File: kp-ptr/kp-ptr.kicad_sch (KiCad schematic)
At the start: 31 parts, among them J1 ESP32_PROG_CON, U1 ESP32-S3, Y1 7M40000005-40MHz

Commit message: One step closer to perfection!
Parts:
- added R76, R77: 1k, Resistor_SMD:R_0402_1005Metric, symbol Device:R
- added R78: 100k, Resistor_SMD:R_0402_1005Metric, symbol Device:R
- added R79, R80: 10k, Resistor_SMD:R_0402_1005Metric, symbol Device:R
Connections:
- net +3V3: now also R78.2, R79.2, R80.2
- net LSM2_INT: now also R79.1
- net LSM_INT: now also R80.1
- net UART1_IN: now also R77.2; no longer U1.19 (GPIO14/ADC2_CH3)
- net UART1_OUT: now also R76.2; no longer U1.18 (GPIO13/ADC2_CH2)
- new net: R76.1, U1.18 (GPIO13/ADC2_CH2)
- new net: R77.1, R78.1, U1.19 (GPIO14/ADC2_CH3)
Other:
- moved on the sheet: R64, R65

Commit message: Parts renumbered! Noice!
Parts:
- renumbered C15 to C10, C4 to C11, C8 to C12, C9 to C13, C10 to C14, C11 to C15, C12 to C3, C13 to C4, C3 to C5, C5 to C6, C6 to C7, C7 to C8, C14 to C9, R79 to R1, R1 to R10, R2 to R11, R3 to R12, R4 to R13, R8 to R14, R5 to R15, R80 to R2, R64 to R3, R65 to R4, R6 to R5, R7 to R6, R76 to R7, R77 to R8, R78 to R9
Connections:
- net IGN1_DET: now also U1.12 (GPIO7/ADC1_CH6); no longer U1.10 (GPIO5/ADC1_CH4)
- net IGN1_EN: now also U1.17 (GPIO12/ADC2_CH1); no longer U1.16 (GPIO11/ADC2_CH0)
- net IGN3_DET: now also U1.10 (GPIO5/ADC1_CH4); no longer U1.12 (GPIO7/ADC1_CH6)
- net IGN3_EN: now also U1.16 (GPIO11/ADC2_CH0); no longer U1.14 (GPIO9/ADC1_CH8)
- net IGN4_EN: now also U1.14 (GPIO9/ADC1_CH8); no longer U1.17 (GPIO12/ADC2_CH1)

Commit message: Wersja produkcyjna v1
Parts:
- C1: value 4pF -> 3.3pF
- C2: value 5pF -> 4.7pF
- L2: value 2nH -> 3.9nH
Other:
- note added: "Optymalnie: 4pF - 1.8nH - 5pF"
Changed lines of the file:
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@@
     (stroke (width 0) (type default) (color 0 0 0 0))
+  )
+  (text "Optymalnie:\n4pF - 1.8nH - 5pF" (at 41.275 40.64 0)
+    (effects (font (size 1.27 1.27)) (justify left bottom))
   )
   (text "https://www.espressif.com/sites/default/files/documentation/esp32-s3_hardware_design_guidelines_en.pdf\nhttps://dl.espressif.com/dl/SCH_ESP32-S3-DEVKITC-1_V1_20210312C.pdf\nhttps://www.espressif.com/sites/default/files/documentation/esp32-s3-wroom-1_wroom-1u_datasheet_en.pdf"
@@
   )
   (symbol (lib_id "Device:L") (at 86.36 125.73 90) (unit 1)
-    (in_bom yes) (on_board yes) (fields_autoplaced)
-    (property "Reference" "L2" (id 0) (at 86.36 119.38 90))
-    (property "Value" "2nH" (id 1) (at 86.36 121.92 90))
+    (in_bom yes) (on_board yes)
+    (property "Reference" "L2" (id 0) (at 86.36 120.65 90))
+    (property "Value" "3.9nH" (id 1) (at 86.36 123.19 90))
     (property "Footprint" "Inductor_SMD:L_0402_1005Metric" (id 2) (at 86.36 125.73 0)
       (effects (font (size 1.27 1.27)) hide)
@@
       (effects (font (size 1.27 1.27)) (justify left))
     )
-    (property "Value" "4pF" (id 1) (at 48.26 53.3399 0)
+    (property "Value" "3.3pF" (id 1) (at 48.26 53.3399 0)
       (effects (font (size 1.27 1.27)) (justify left))
     )
@@
       (effects (font (size 1.27 1.27)) (justify left))
     )
-    (property "Value" "5pF" (id 1) (at 59.69 53.3399 0)
+    (property "Value" "4.7pF" (id 1) (at 59.69 53.3399 0)
       (effects (font (size 1.27 1.27)) (justify left))
     )
@@
     )
     (path "/8ef1d6c2-9afb-467f-94f0-2a571e5715a1"
-      (reference "C1") (unit 1) (value "4pF") (footprint "Capacitor_SMD:C_0402_1005Metric")
+      (reference "C1") (unit 1) (value "3.3pF") (footprint "Capacitor_SMD:C_0402_1005Metric")
     )
     (path "/9fcdb267-77a5-4e61-b2de-f64dc52ca3df"
-      (reference "C2") (unit 1) (value "5pF") (footprint "Capacitor_SMD:C_0402_1005Metric")
+      (reference "C2") (unit 1) (value "4.7pF") (footprint "Capacitor_SMD:C_0402_1005Metric")
     )
     (path "/110ce750-0b6b-4572-b83f-b69947a7115a"
@@
     )
     (path "/f38dad53-0af4-40f6-a173-e0e37aecb5da/2de207c9-9c33-4eda-813e-68639dee740f"
-      (reference "C45") (unit 1) (value "390pF") (footprint "Capacitor_SMD:C_0402_1005Metric")
+      (reference "C45") (unit 1) (value "470pF") (footprint "Capacitor_SMD:C_0402_1005Metric")
     )
     (path "/5f9da060-2eb0-4ae6-ad5b-b0da419a62a6/6c16042f-ade1-413e-a421-4ab855737deb"
@@
     )
     (path "/f38dad53-0af4-40f6-a173-e0e37aecb5da/0c823417-32f1-463d-9866-2207d5ddc049"
-      (reference "D5") (unit 1) (value "G") (footprint "LED_SMD:LED_0603_1608Metric")
+      (reference "D5") (unit 1) (value "GREEN") (footprint "LED_SMD:LED_0603_1608Metric")
     )
     (path "/f38dad53-0af4-40f6-a173-e0e37aecb5da/2276f1f5-93b0-425f-83ff-bcbfd5842553"
-      (reference "D6") (unit 1) (value "G") (footprint "LED_SMD:LED_0603_1608Metric")
+      (reference "D6") (unit 1) (value "GREEN") (footprint "LED_SMD:LED_0603_1608Metric")
     )
     (path "/f38dad53-0af4-40f6-a173-e0e37aecb5da/cf119e5f-57a5-45a3-9444-d091235884b3"
-      (reference "D7") (unit 1) (value "G") (footprint "LED_SMD:LED_0603_1608Metric")
+      (reference "D7") (unit 1) (value "GREEN") (footprint "LED_SMD:LED_0603_1608Metric")
     )
     (path "/5f9da060-2eb0-4ae6-ad5b-b0da419a62a6/94e53db9-ffab-45c9-951c-83988bceb04a"
@@
     )
     (path "/5f9da060-2eb0-4ae6-ad5b-b0da419a62a6/db5a8438-b89c-4b0b-b76a-192cb9089c1f"
-      (reference "D9") (unit 1) (value "LED") (footprint "LED_SMD:LED_0603_1608Metric")
+      (reference "D9") (unit 1) (value "BLUE") (footprint "LED_SMD:LED_0603_1608Metric")
     )
     (path "/68d9bec4-a8fa-482b-99d8-a42578238d37/f1919372-4fb4-4ad7-b8a4-d25a131d4571"
@@
     )
     (path "/68d9bec4-a8fa-482b-99d8-a42578238d37/7419015c-d6f5-473a-81b5-0c1550cbc74a"
-      (reference "D15") (unit 1) (value "LED") (footprint "LED_SMD:LED_0603_1608Metric")
+      (reference "D15") (unit 1) (value "GREEN") (footprint "LED_SMD:LED_0603_1608Metric")
     )
     (path "/68d9bec4-a8fa-482b-99d8-a42578238d37/756827ed-712a-45c9-ae4c-3582ec9796b1"
@@
     )
     (path "/1d5e7912-4d51-4a4c-b45e-2695b4191d61/267f3f5c-5986-42a8-90e0-9867572b9498"
-      (reference "FB1") (unit 1) (value "200mA") (footprint "Resistor_SMD:R_0402_1005Metric")
+      (reference "FB1") (unit 1) (value "GZ1608D601TF") (footprint "Resistor_SMD:R_0603_1608Metric")
     )
     (path "/5f9da060-2eb0-4ae6-ad5b-b0da419a62a6/aa98c128-9952-4c14-a652-c12ef28a16e3"
-      (reference "FB2") (unit 1) (value "1000mA") (footprint "Resistor_SMD:R_0603_1608Metric")
+      (reference "FB2") (unit 1) (value "GZ1608D601TF") (footprint "Resistor_SMD:R_0603_1608Metric")
     )
     (path "/f38dad53-0af4-40f6-a173-e0e37aecb5da/8c9be223-3e3b-4263-be76-100d6db5c98e"
-      (reference "IC1") (unit 1) (value "TPS62140ARGTR") (footprint "KP-PTR_lib:QFN50P300X300X100-17N-D")
+      (reference "IC1") (unit 1) (value "TPS62140RGTR") (footprint "KP-PTR_lib:QFN50P300X300X100-17N-D")
     )
     (path "/5f9da060-2eb0-4ae6-ad5b-b0da419a62a6/82aae44a-c9ee-4277-9258-adb407e6a613"
@@
     )
     (path "/0b968d3c-2563-4a21-9c01-33df722d100e"
-      (reference "L2") (unit 1) (value "2nH") (footprint "Inductor_SMD:L_0402_1005Metric")
+      (reference "L2") (unit 1) (value "3.9nH") (footprint "Inductor_SMD:L_0402_1005Metric")
     )
     (path "/1d5e7912-4d51-4a4c-b45e-2695b4191d61/4255a2b2-c667-497c-8694-71ada229b2f2"
@@
     )
     (path "/1d5e7912-4d51-4a4c-b45e-2695b4191d61/cd4ecd76-e91e-4533-a74a-34ce1b622583"
-      (reference "R20") (unit 1) (value "4k7") (footprint "Resistor_SMD:R_0402_1005Metric")
+      (reference "R20") (unit 1) (value "10k") (footprint "Resistor_SMD:R_0402_1005Metric")
     )
     (path "/1d5e7912-4d51-4a4c-b45e-2695b4191d61/d1275fb6-d548-486b-a6ee-dbd1cec8a8ca"
@@
     )
     (path "/f38dad53-0af4-40f6-a173-e0e37aecb5da/40f1fe21-813f-46d5-8590-192f81966584"
-      (reference "R34") (unit 1) (value "562k 1%") (footprint "Resistor_SMD:R_0402_1005Metric")
+      (reference "R34") (unit 1) (value "470k 1%") (footprint "Resistor_SMD:R_0402_1005Metric")
     )
     (path "/f38dad53-0af4-40f6-a173-e0e37aecb5da/432a6cc6-fa1b-4a12-a5bc-555c3130a65e"
-      (reference "R35") (unit 1) (value "180k 1%") (footprint "Resistor_SMD:R_0402_1005Metric")
+      (reference "R35") (unit 1) (value "150k 1%") (footprint "Resistor_SMD:R_0402_1005Metric")
     )
     (path "/5f9da060-2eb0-4ae6-ad5b-b0da419a62a6/c794e615-91d9-4c55-bccb-75991bf3c5d7"
@@
     )
     (path "/5f9da060-2eb0-4ae6-ad5b-b0da419a62a6/1c848c44-17b3-4d34-873f-72b55ac056a2"
-      (reference "U12") (unit 1) (value "NL27WZU04DBVT1G") (footprint "KP-PTR_lib:SOT95P275X110-6N")
+      (reference "U12") (unit 1) (value "NL27WZU04DBVT1G") (footprint "Package_TO_SOT_SMD:SOT-363_SC-70-6")
     )
     (path "/5f9da060-2eb0-4ae6-ad5b-b0da419a62a6/835aef12-4bff-4866-8baa-53c89c7073f7"

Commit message: Release v1
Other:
- note removed: "Dodać wyprowadznie paska LED"
- company: (none) -> Polskie Towarzystwo Rakietowe
- title: (none) -> KP-PTR
- moved on the sheet: C11, C12, C13, C14, C15, R15

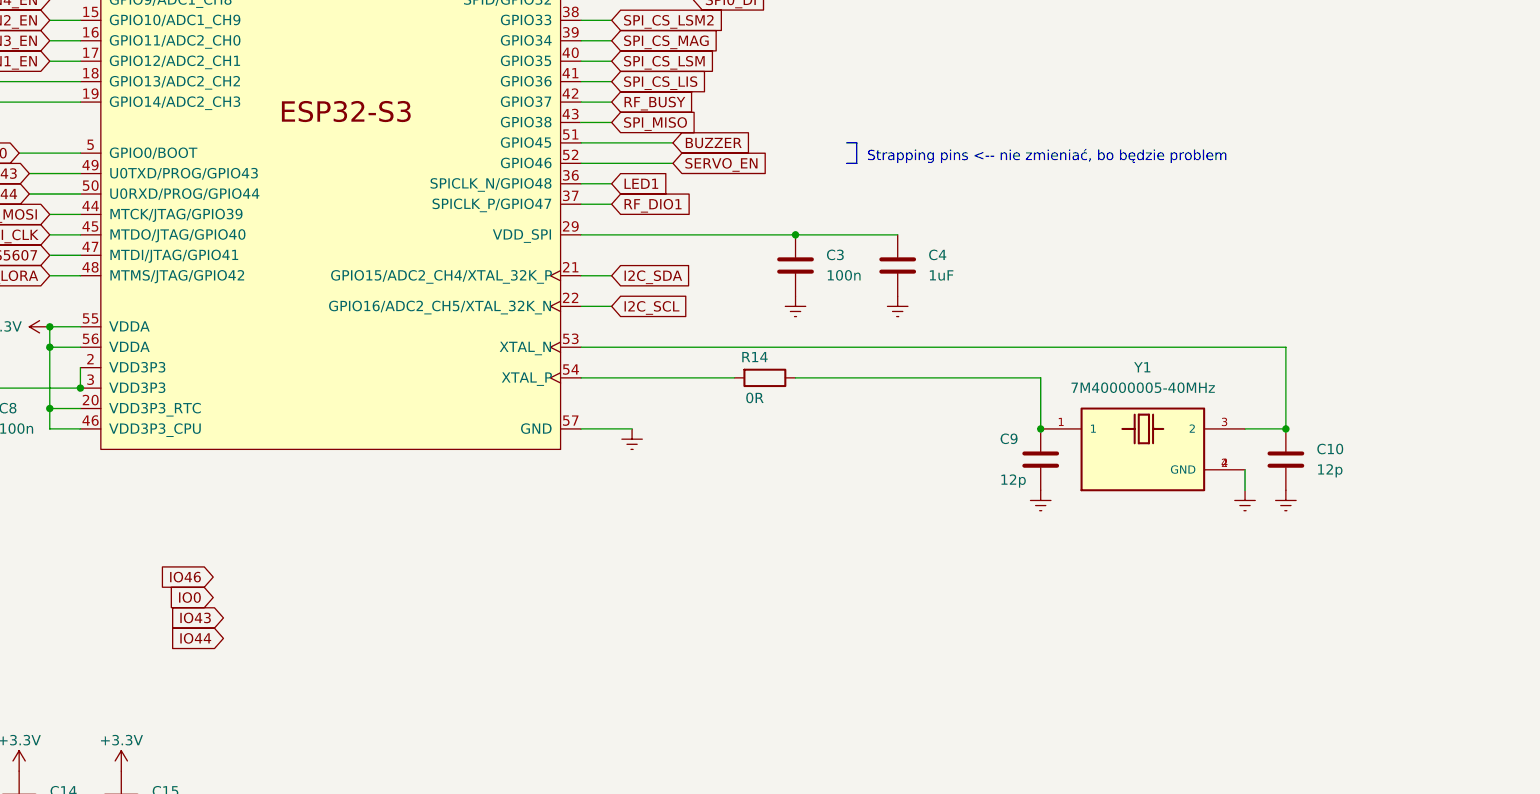
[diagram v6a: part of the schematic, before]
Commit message: New schematic revision v1.1:
- added 'DNP' info for few components
- some stylistic improvements
- added comment about I2C pins glitch
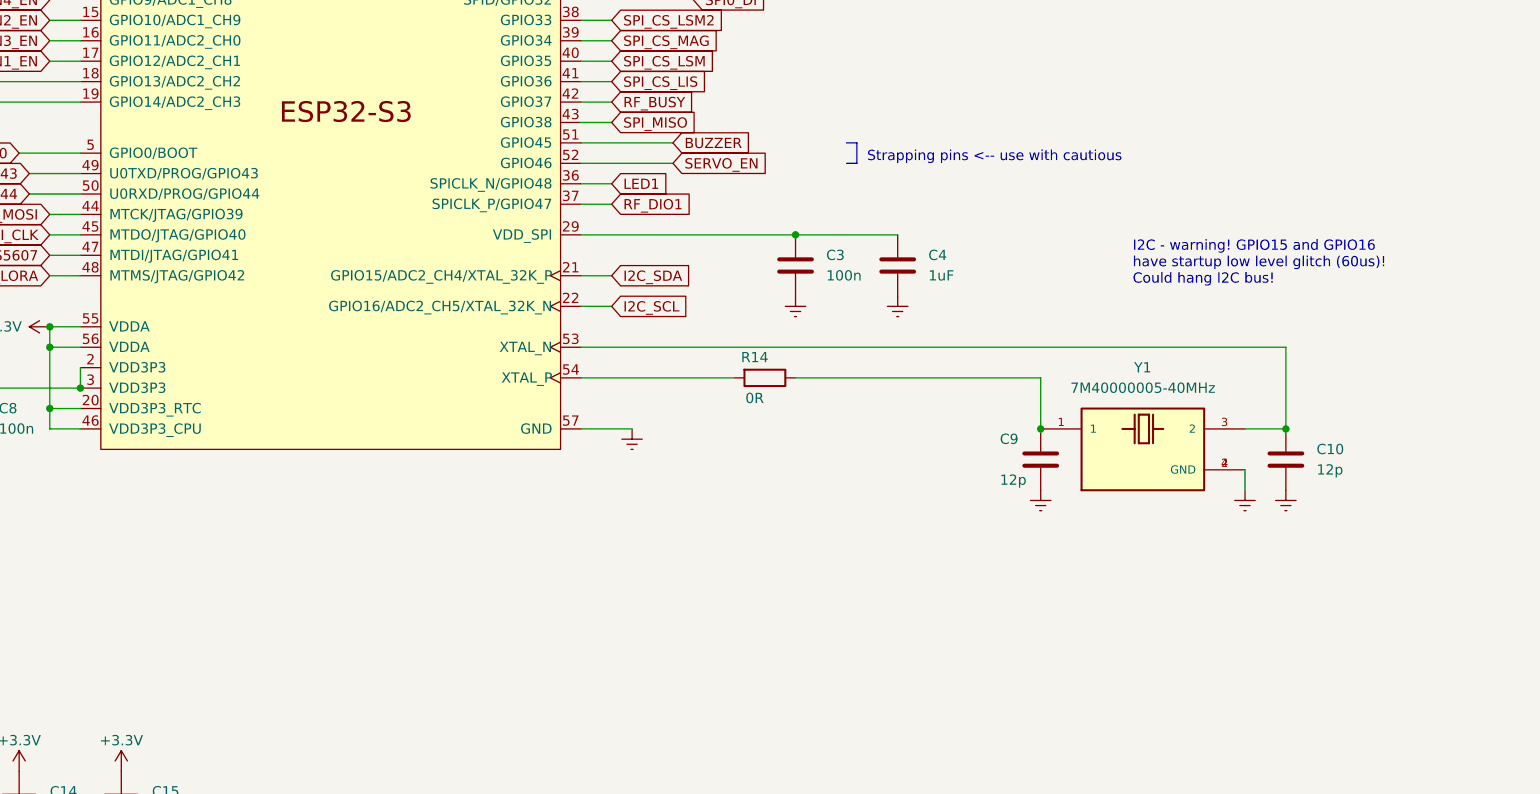
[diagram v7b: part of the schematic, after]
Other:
- note added: "I2C - warning! GPIO15 and GPIO16 have startup low level glitch (60us)! Could hang I2C bus!"
- note added: "Strapping pins <-- use with cautious"
- note removed: "Strapping pins <-- nie zmieniać, bo będzie problem"
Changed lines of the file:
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@@
   (title_block
     (title "KP-PTR")
-    (date "2022-11-18")
-    (rev "1")
+    (date "2023-12-10")
+    (rev "1.1")
     (company "Polskie Towarzystwo Rakietowe")
     (comment 1 "bartekM, FlyingBanana, Kretu, Red Labs, Stachu M, U.S. air force i inni")
@@
     (effects (font (size 1.27 1.27)) (justify left bottom))
   )
+  (text "I2C - warning! GPIO15 and GPIO16 \nhave startup low level glitch (60us)!\nCould hang I2C bus!"
+    (at 240.03 113.03 0)
+    (effects (font (size 1.27 1.27)) (justify left bottom))
+  )
   (text "50 Ohm" (at 71.12 48.26 0)
     (effects (font (size 1.27 1.27)) (justify left bottom))
@@
     (effects (font (size 1.27 1.27)) (justify left bottom))
   )
-  (text "Strapping pins <-- nie zmieniać, bo będzie problem"
-    (at 207.01 97.79 0)
+  (text "Strapping pins <-- use with cautious" (at 207.01 97.79 0)
     (effects (font (size 1.27 1.27)) (justify left bottom))
   )
@@
     )
   )
-  (global_label "IO46" (shape input) (at 125.73 149.225 180) (fields_autoplaced)
-    (effects (font (size 1.27 1.27)) (justify right))
-    (property "Intersheet References" "${INTERSHEET_REFS}" (id 0) (at 118.9626 149.3044 0)
-      (effects (font (size 1.27 1.27)) (justify right) hide)
-    )
-  )
   (global_label "I2C_SDA" (shape input) (at 175.26 111.76 0) (fields_autoplaced)
     (effects (font (size 1.27 1.27)) (justify left))
@@
     )
   )
-  (global_label "IO0" (shape input) (at 125.73 151.765 180) (fields_autoplaced)
-    (effects (font (size 1.27 1.27)) (justify right))
-    (property "Intersheet References" "${INTERSHEET_REFS}" (id 0) (at 120.1721 151.6856 0)
-      (effects (font (size 1.27 1.27)) (justify right) hide)
-    )
-  )
   (global_label "IO43" (shape input) (at 65.405 111.76 0) (fields_autoplaced)
     (effects (font (size 1.27 1.27)) (justify left))
@@
     )
   )
-  (global_label "IO43" (shape input) (at 127 154.305 180) (fields_autoplaced)
-    (effects (font (size 1.27 1.27)) (justify right))
-    (property "Intersheet References" "${INTERSHEET_REFS}" (id 0) (at 120.2326 154.2256 0)
-      (effects (font (size 1.27 1.27)) (justify right) hide)
-    )
-  )
   (global_label "LSM2_INT" (shape input) (at 234.95 39.37 0) (fields_autoplaced)
     (effects (font (size 1.27 1.27)) (justify left))
@@
     )
   )
-  (global_label "IO44" (shape input) (at 127 156.845 180) (fields_autoplaced)
-    (effects (font (size 1.27 1.27)) (justify right))
-    (property "Intersheet References" "${INTERSHEET_REFS}" (id 0) (at 120.2326 156.7656 0)
-      (effects (font (size 1.27 1.27)) (justify right) hide)
-    )
-  )
   (global_label "RF_BUSY" (shape input) (at 175.26 90.17 0) (fields_autoplaced)
     (effects (font (size 1.27 1.27)) (justify left))
@@
     )
     (path "/1d5e7912-4d51-4a4c-b45e-2695b4191d61/1d256433-6de4-4c3c-8bf6-473c8fb18526"
-      (reference "C29") (unit 1) (value "TBD") (footprint "Capacitor_SMD:C_0402_1005Metric")
+      (reference "C29") (unit 1) (value "DNP") (footprint "Capacitor_SMD:C_0402_1005Metric")
     )
     (path "/1d5e7912-4d51-4a4c-b45e-2695b4191d61/cb8b5a4d-f53c-4fdd-bbba-ccb732fe5d61"
-      (reference "C30") (unit 1) (value "1nF") (footprint "Capacitor_SMD:C_0402_1005Metric")
+      (reference "C30") (unit 1) (value "DNP") (footprint "Capacitor_SMD:C_0402_1005Metric")
     )
     (path "/1d5e7912-4d51-4a4c-b45e-2695b4191d61/e96c3e2a-2126-4340-898b-967da0484374"
@@
     )
     (path "/1d5e7912-4d51-4a4c-b45e-2695b4191d61/ffd6a983-4822-4f37-978e-177b7febe08c"
-      (reference "D2") (unit 1) (value "TBD") (footprint "Diode_SMD:D_0402_1005Metric")
+      (reference "D2") (unit 1) (value "DNP") (footprint "Diode_SMD:D_0402_1005Metric")
     )
     (path "/f38dad53-0af4-40f6-a173-e0e37aecb5da/55b5f7c1-9e27-4de8-8da9-4ddd7c634c2f"
@@
     )
     (path "/5f9da060-2eb0-4ae6-ad5b-b0da419a62a6/82aae44a-c9ee-4277-9258-adb407e6a613"
-      (reference "IC2") (unit 1) (value "E22-900M22S") (footprint "KP-PTR_lib:E22-900M22S")
+      (reference "IC2") (unit 1) (value "E22-400M22S") (footprint "KP-PTR_lib:E22-900M22S")
     )
     (path "/a069c936-1b73-4515-a7dd-c3cee8aa8158"
@@
     )
     (path "/1d5e7912-4d51-4a4c-b45e-2695b4191d61/4255a2b2-c667-497c-8694-71ada229b2f2"
-      (reference "L3") (unit 1) (value "10nH") (footprint "Inductor_SMD:L_0402_1005Metric")
+      (reference "L3") (unit 1) (value "DNP") (footprint "Inductor_SMD:L_0402_1005Metric")
     )
     (path "/f38dad53-0af4-40f6-a173-e0e37aecb5da/eafe2b3b-29a9-4552-bf6b-b6b9a49759ba"
@@
     )
     (path "/1d5e7912-4d51-4a4c-b45e-2695b4191d61/08102467-11bf-4118-8a9a-4b9393fed23f"
-      (reference "R24") (unit 1) (value "100R") (footprint "Resistor_SMD:R_0402_1005Metric")
+      (reference "R24") (unit 1) (value "DNP") (footprint "Resistor_SMD:R_0402_1005Metric")
     )
     (path "/1d5e7912-4d51-4a4c-b45e-2695b4191d61/1820113b-b3c5-414e-a854-423480a843b7"
@@
     )
     (path "/1d5e7912-4d51-4a4c-b45e-2695b4191d61/b1cb46aa-37b1-44bf-9609-48e120b6c51d"
-      (reference "R26") (unit 1) (value "10k") (footprint "Resistor_SMD:R_0402_1005Metric")
+      (reference "R26") (unit 1) (value "DNP") (footprint "Resistor_SMD:R_0402_1005Metric")
     )
     (path "/f38dad53-0af4-40f6-a173-e0e37aecb5da/02ab2548-d360-4d53-ba49-ccf0853e38ce"
@@
     )
     (path "/1d5e7912-4d51-4a4c-b45e-2695b4191d61/8e687858-1f88-4aa6-9fdc-2f0ed3726595"
-      (reference "U7") (unit 1) (value "NJG1156PCD") (footprint "KP-PTR_lib:SON50P260X260X55-11N")
+      (reference "U7") (unit 1) (value "DNP") (footprint "KP-PTR_lib:SON50P260X260X55-11N")
     )
     (path "/1d5e7912-4d51-4a4c-b45e-2695b4191d61/2f079120-278f-4a48-8d65-52cce2941b14"
@@
     )
     (path "/f38dad53-0af4-40f6-a173-e0e37aecb5da/526d0603-75ac-4309-8a51-6c753b790387"
-      (reference "U9") (unit 1) (value "LDFM33PVR") (footprint "KP-PTR_lib:LDFM33PVR")
+      (reference "U9") (unit 1) (value "DNP") (footprint "KP-PTR_lib:LDFM33PVR")
     )
     (path "/f38dad53-0af4-40f6-a173-e0e37aecb5da/814893a8-2bf5-4f5e-b499-9964c8084e05"
